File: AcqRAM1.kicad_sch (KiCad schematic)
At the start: 241 parts, among them U25 MSM5416283, U26 MSM5416283, U27 MSM5416283, U28 MSM5416283, U29 MSM5416283, U35 MSM5416283, U36 MSM5416283, U37 MSM5416283, U38 MSM5416283, U46 MSM5416283, U47 MSM5416283, U48 MSM5416283, U49 MSM5416283, U54 MSM5416283, U55 MSM5416283, U56 MSM5416283, U57 MSM5416283

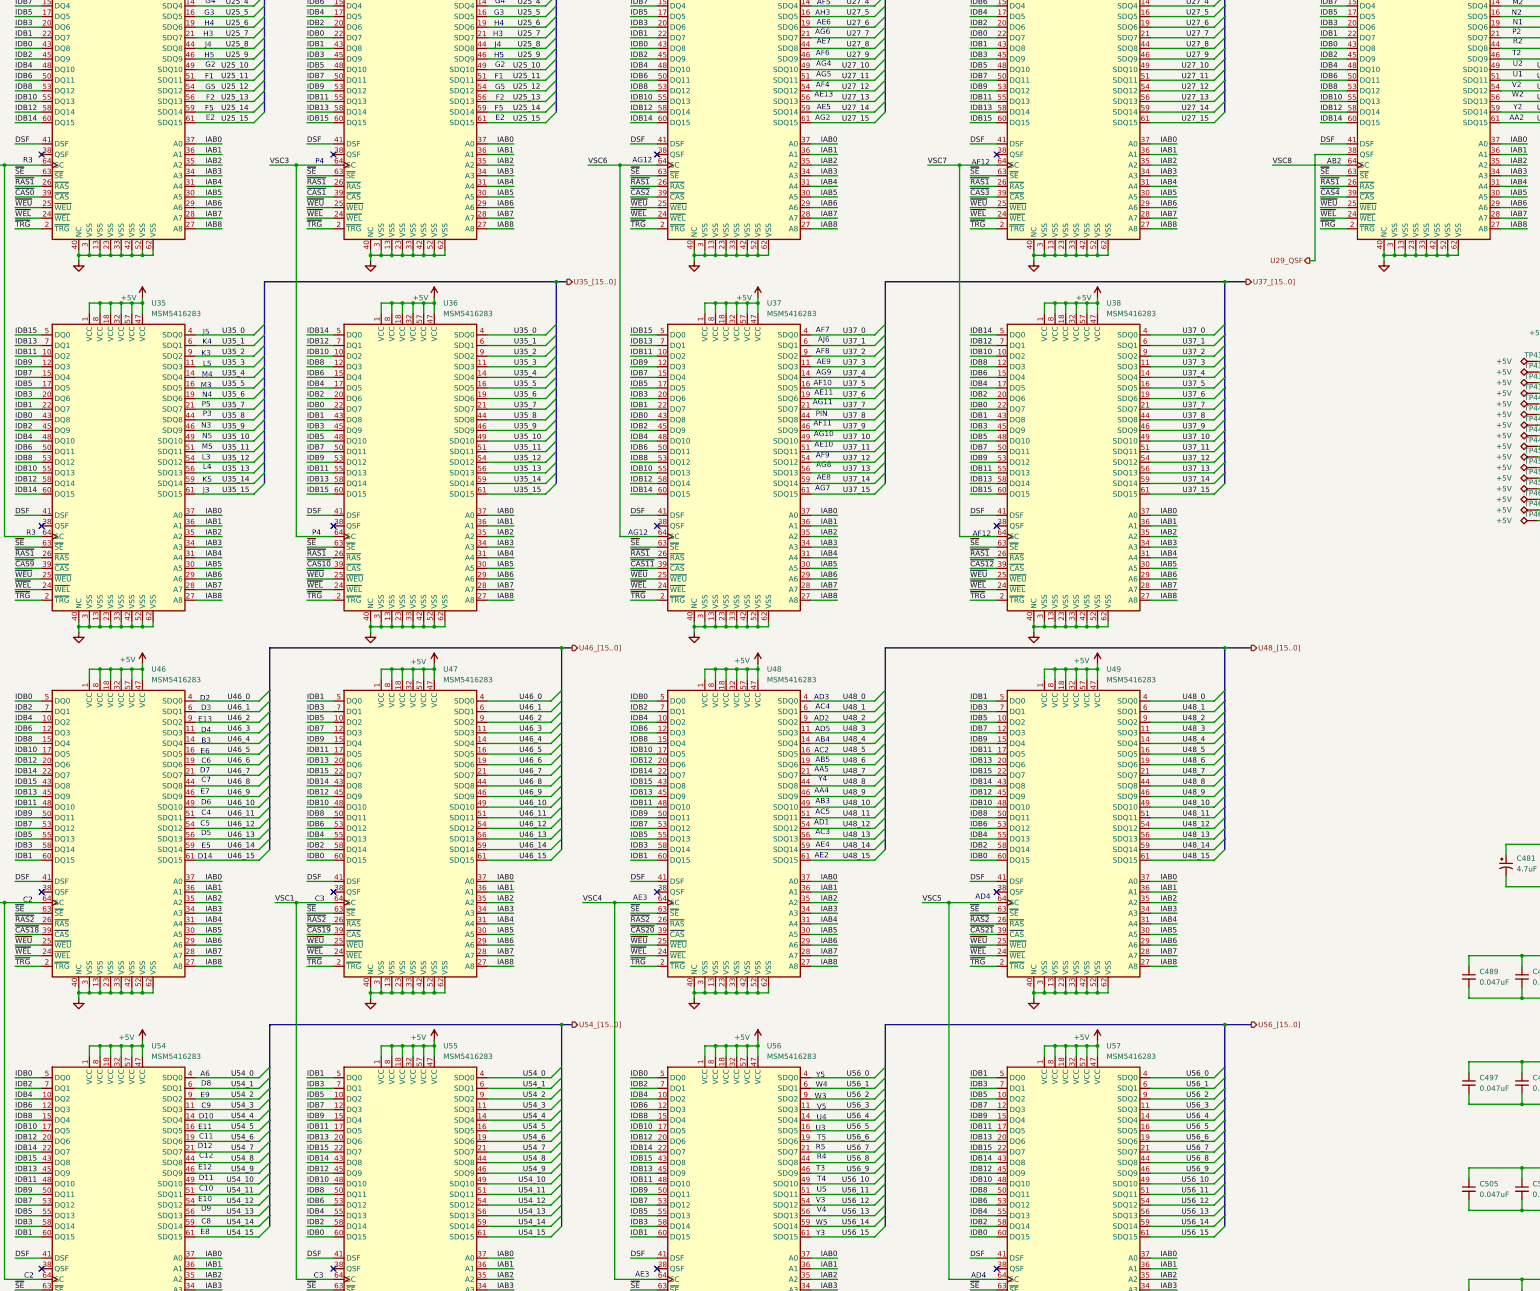
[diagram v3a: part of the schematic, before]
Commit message: Add pv names to VRAM chips
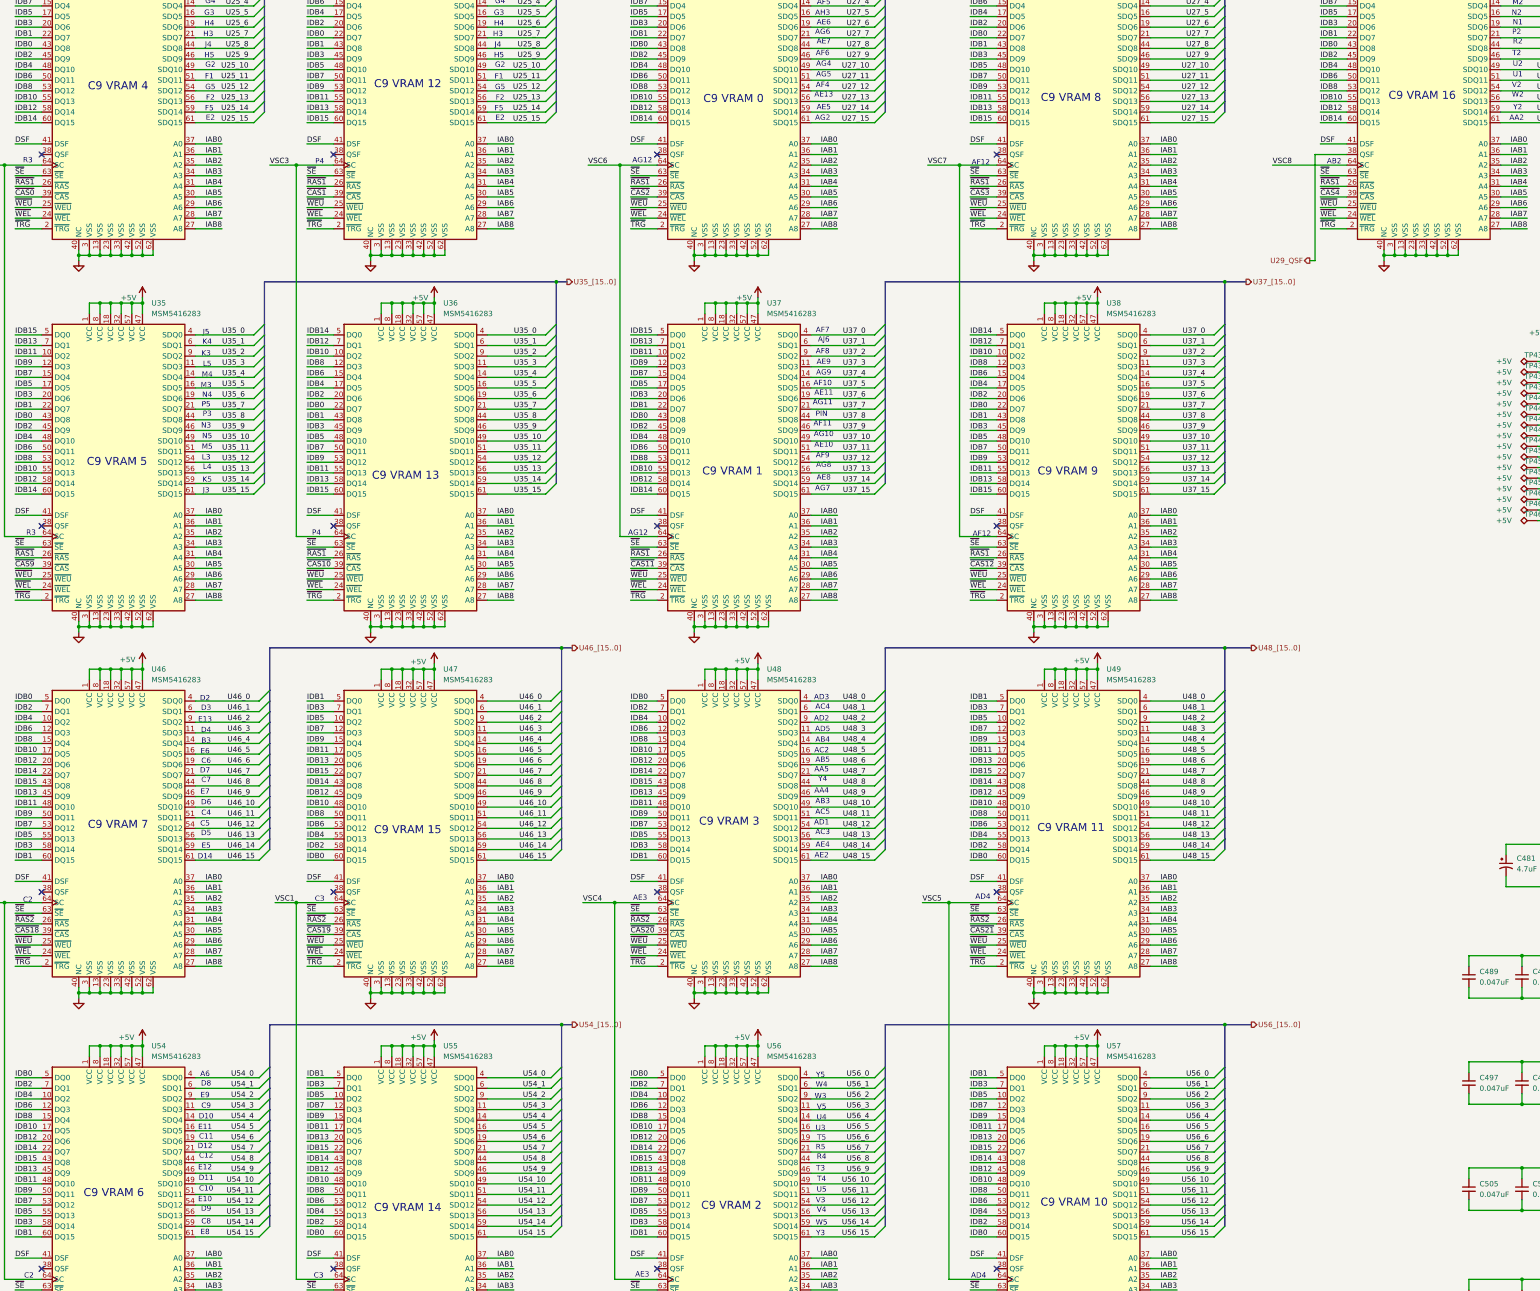
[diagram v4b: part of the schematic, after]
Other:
- note added: "C9 VRAM 0"
- note added: "C9 VRAM 1"
- note added: "C9 VRAM 10"
- note added: "C9 VRAM 11"
- note added: "C9 VRAM 12"
- note added: "C9 VRAM 13"
- note added: "C9 VRAM 14"
- note added: "C9 VRAM 15"
- note added: "C9 VRAM 16"
- note added: "C9 VRAM 2"
- note added: "C9 VRAM 3"
- note added: "C9 VRAM 4"
- note added: "C9 VRAM 5"
- note added: "C9 VRAM 6"
- note added: "C9 VRAM 7"
- note added: "C9 VRAM 8"
- note added: "C9 VRAM 9"
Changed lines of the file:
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@@
 	(generator_version "9.0")
 	(paper "A2")
+	(text "C9 VRAM 2"
+		(exclude_from_sim no)
+		(at 271.78 324.104 0)
+		(effects
+			(font
+				(size 1.905 1.905)
+			)
+		)
+	)
 	(text "E7"
 		(exclude_from_sim no)
@@
 		)
 	)
+	(text "C9 VRAM 8"
+		(exclude_from_sim no)
+		(at 353.06 58.928 0)
+		(effects
+			(font
+				(size 1.905 1.905)
+			)
+		)
+	)
 	(text "K4"
 		(exclude_from_sim no)
@@
 		)
 	)
+	(text "C9 VRAM 14"
+		(exclude_from_sim no)
+		(at 194.31 324.612 0)
+		(effects
+			(font
+				(size 1.905 1.905)
+			)
+		)
+	)
 	(text "C3"
 		(exclude_from_sim no)
@@
 		)
 	)
+	(text "C9 VRAM 13"
+		(exclude_from_sim no)
+		(at 193.802 149.352 0)
+		(effects
+			(font
+				(size 1.905 1.905)
+			)
+		)
+	)
 	(text "F4"
 		(exclude_from_sim no)
@@
 		)
 	)
+	(text "C9 VRAM 6"
+		(exclude_from_sim no)
+		(at 123.952 321.056 0)
+		(effects
+			(font
+				(size 1.905 1.905)
+			)
+		)
+	)
 	(text "C10"
 		(exclude_from_sim no)
@@
 		)
 	)
+	(text "C9 VRAM 4"
+		(exclude_from_sim no)
+		(at 124.968 56.134 0)
+		(effects
+			(font
+				(size 1.905 1.905)
+			)
+		)
+	)
+	(text "C9 VRAM 1"
+		(exclude_from_sim no)
+		(at 272.034 148.336 0)
+		(effects
+			(font
+				(size 1.905 1.905)
+			)
+		)
+	)
 	(text "F1"
 		(exclude_from_sim no)
@@
 		)
 	)
+	(text "C9 VRAM 11"
+		(exclude_from_sim no)
+		(at 353.06 233.68 0)
+		(effects
+			(font
+				(size 1.905 1.905)
+			)
+		)
+	)
 	(text "H2"
 		(exclude_from_sim no)
@@
 		)
 	)
+	(text "C9 VRAM 0"
+		(exclude_from_sim no)
+		(at 272.288 59.182 0)
+		(effects
+			(font
+				(size 1.905 1.905)
+			)
+		)
+	)
 	(text "P5"
 		(exclude_from_sim no)
@@
 		)
 	)
+	(text "C9 VRAM 16"
+		(exclude_from_sim no)
+		(at 437.134 58.42 0)
+		(effects
+			(font
+				(size 1.905 1.905)
+			)
+		)
+	)
 	(text "W3"
 		(exclude_from_sim no)
@@
 		)
 	)
+	(text "C9 VRAM 7"
+		(exclude_from_sim no)
+		(at 124.968 232.918 0)
+		(effects
+			(font
+				(size 1.905 1.905)
+			)
+		)
+	)
+	(text "C9 VRAM 10"
+		(exclude_from_sim no)
+		(at 353.822 323.342 0)
+		(effects
+			(font
+				(size 1.905 1.905)
+			)
+		)
+	)
 	(text "D4"
 		(exclude_from_sim no)
@@
 		)
 	)
+	(text "C9 VRAM 3"
+		(exclude_from_sim no)
+		(at 271.272 232.156 0)
+		(effects
+			(font
+				(size 1.905 1.905)
+			)
+		)
+	)
 	(text "PIN"
 		(exclude_from_sim no)
@@
 		)
 	)
+	(text "C9 VRAM 15"
+		(exclude_from_sim no)
+		(at 194.31 234.188 0)
+		(effects
+			(font
+				(size 1.905 1.905)
+			)
+		)
+	)
 	(text "W2"
 		(exclude_from_sim no)
@@
 		)
 	)
+	(text "C9 VRAM 5"
+		(exclude_from_sim no)
+		(at 124.714 146.05 0)
+		(effects
+			(font
+				(size 1.905 1.905)
+			)
+		)
+	)
+	(text "C9 VRAM 12"
+		(exclude_from_sim no)
+		(at 194.31 55.626 0)
+		(effects
+			(font
+				(size 1.905 1.905)
+			)
+		)
+	)
 	(text "F3"
 		(exclude_from_sim no)
@@
 			)
 		)
+	)
+	(text "C9 VRAM 9"
+		(exclude_from_sim no)
+		(at 352.298 148.336 0)
+		(effects
+			(font
+				(size 1.905 1.905)
+			)
+		)
